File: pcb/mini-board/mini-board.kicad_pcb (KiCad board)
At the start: 4 copper layers, 132.1 x 132.1 mm, 55 parts, among them J1 USB_B, J2 EXPANSION BUS, J3 SD Card Board, J4 Atmel-JTAG-10, J5 SYSTEM BUS, J8 SERIAL, SW1 SW_SPDT, SW2 RESET, SW3 NMI, U1 74AC11, U11 DS1813, U15 SST39SF040, U16 AS6C4008-55, U19 W65C22S, U2 W65C02, U21 W65C51N, U22 MAX232, U23 ATF1502AS, X1 CLK, Y1 1.8432 MHz

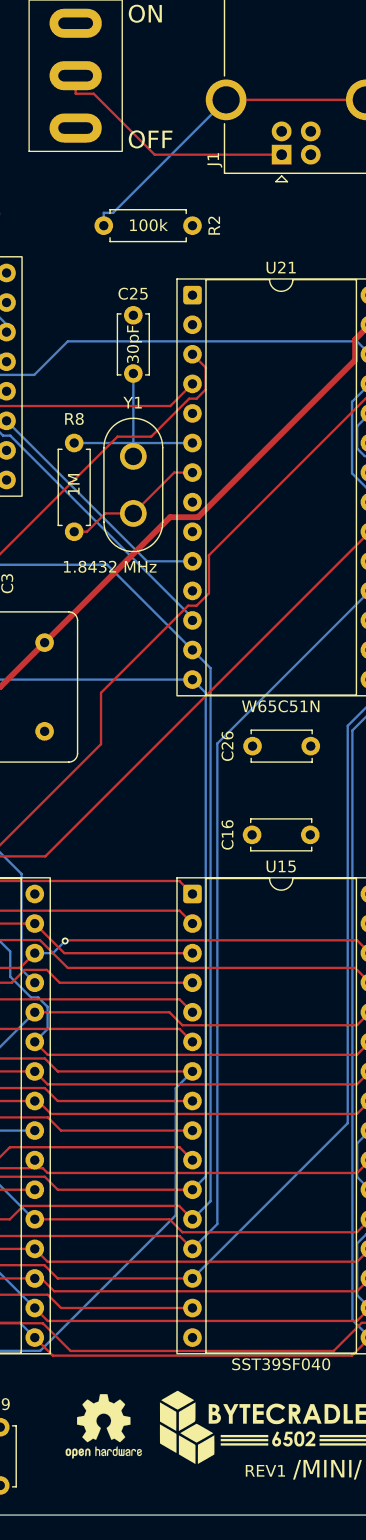
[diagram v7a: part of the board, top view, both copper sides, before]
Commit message: Fixing width of VIN
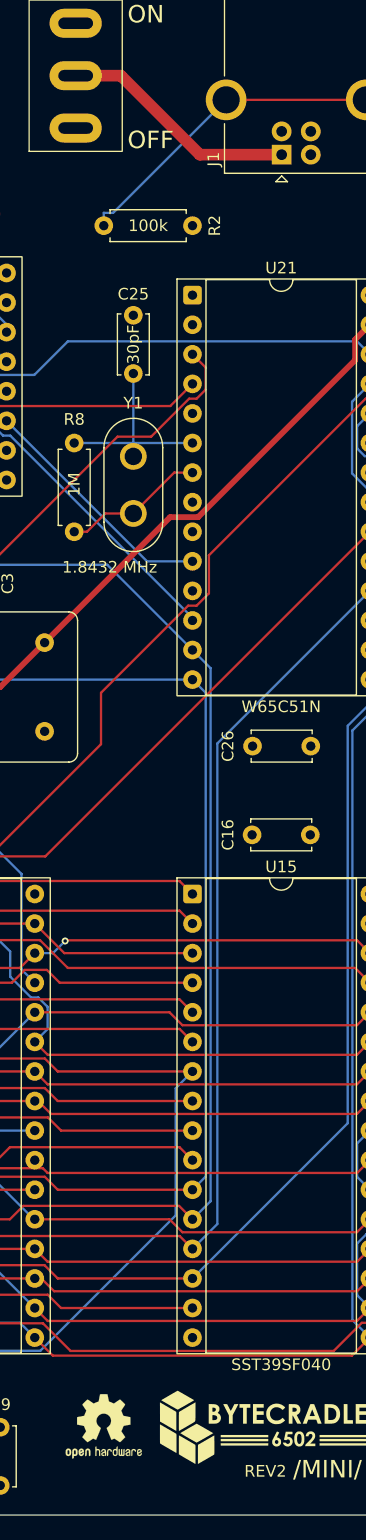
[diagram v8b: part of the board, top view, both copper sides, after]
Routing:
- net VIN: track 21.4 -> 20.5 mm
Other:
- board text added: "REV2"
- board text removed: "REV1"
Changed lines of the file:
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@@
 			(psa4output no)
 			(plot_black_and_white yes)
-			(plotinvisibletext no)
 			(sketchpadsonfab no)
 			(plotpadnumbers no)
@@
 		)
 	)
-	(gr_text "REV1"
+	(gr_text "REV2"
 		(at 238.125 154.305 0)
 		(layer "F.SilkS")
@@
 	)
 	(segment
-		(start 241.34 40.64)
-		(end 230.433 40.64)
-		(width 0.2)
-		(layer "F.Cu")
-		(net 67)
-	)
-	(segment
-		(start 223.647 33.854)
-		(end 223.647 35.4041)
-		(width 0.2)
+		(start 234.315 40.64)
+		(end 227.529 33.854)
+		(width 1)
 		(layer "F.Cu")
 		(net 67)
 	)
 	(segment
-		(start 225.1971 35.4041)
-		(end 223.647 35.4041)
-		(width 0.2)
+		(start 227.529 33.854)
+		(end 223.647 33.854)
+		(width 1)
 		(layer "F.Cu")
 		(net 67)
 	)
 	(segment
-		(start 230.433 40.64)
-		(end 225.1971 35.4041)
-		(width 0.2)
+		(start 241.34 40.64)
+		(end 234.315 40.64)
+		(width 1)
 		(layer "F.Cu")
 		(net 67)
